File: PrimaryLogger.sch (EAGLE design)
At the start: 55 parts, among them J1 CONN_42.54_SCREW, J2 CONN_42.54_SCREW, J3 CONN_42.54_SCREW, J4 CONN_42.54_SCREW, J5 CONN_32.54_SCREW, Q1 DMG3404, Q2 DMG3404, U1 MIC2005, U2 MIC2091, U25 SN74AUP3G34DCU, U3 TPL5010DDC, U4 TXS0102DCU, U5 SN74LVC1G3157DRL, U6 TCS3400, U7 SHTC3DFN, U8 MCP23008QFN, U9 MCP7940SOIC

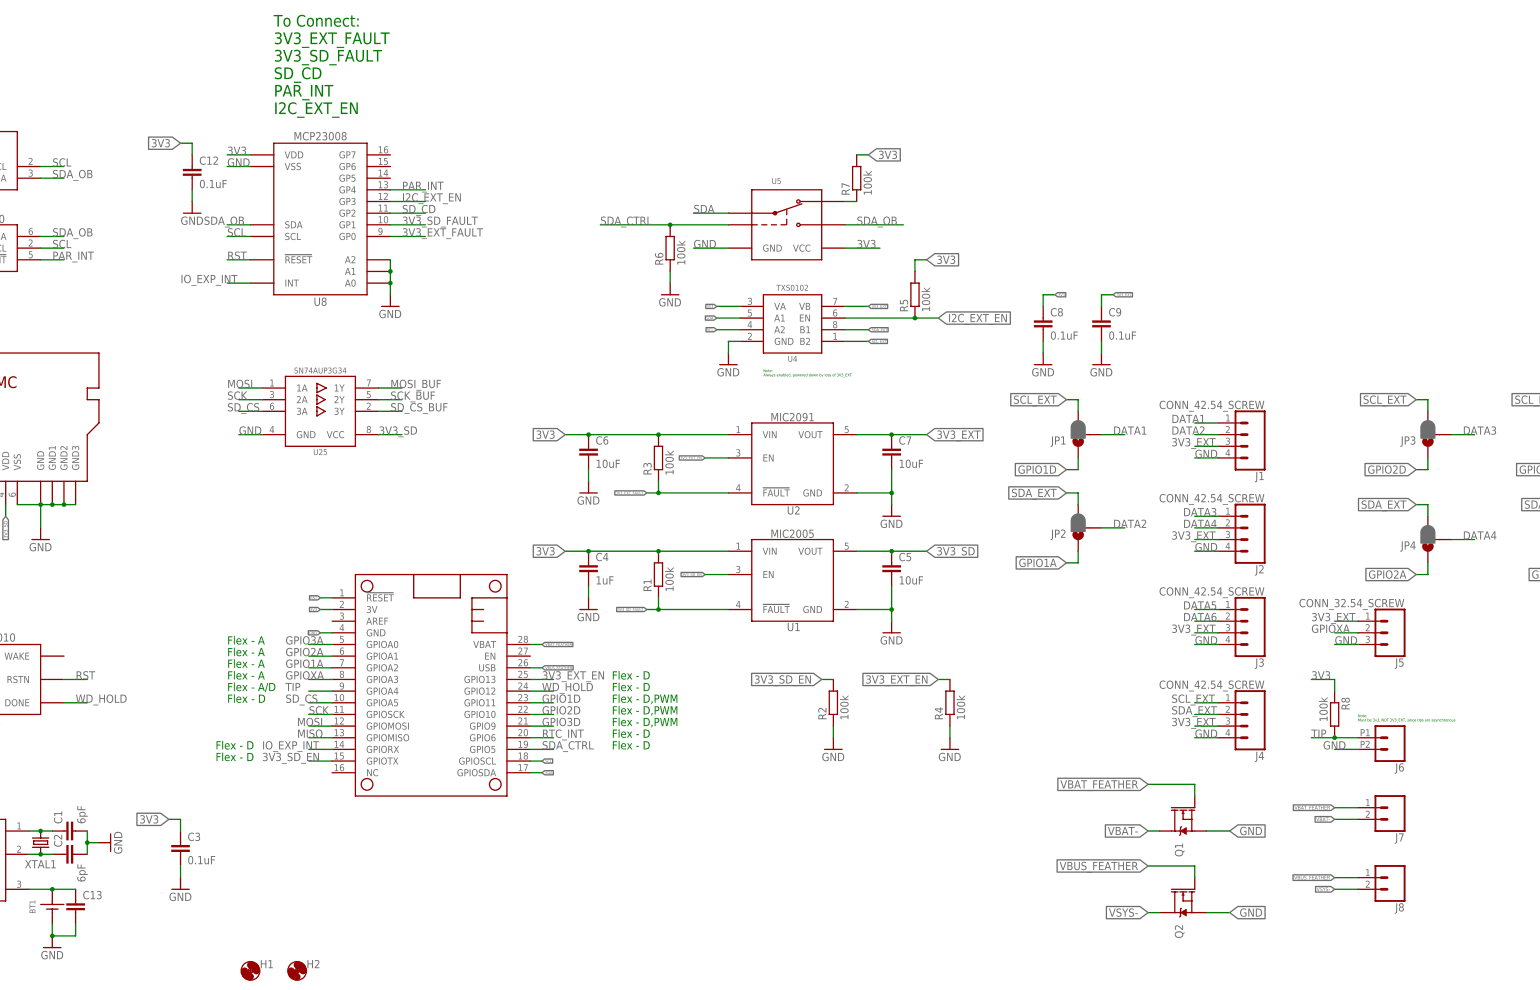
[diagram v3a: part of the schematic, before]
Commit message: Minor updates to layout
Added silk screen, added test points, other minor edits
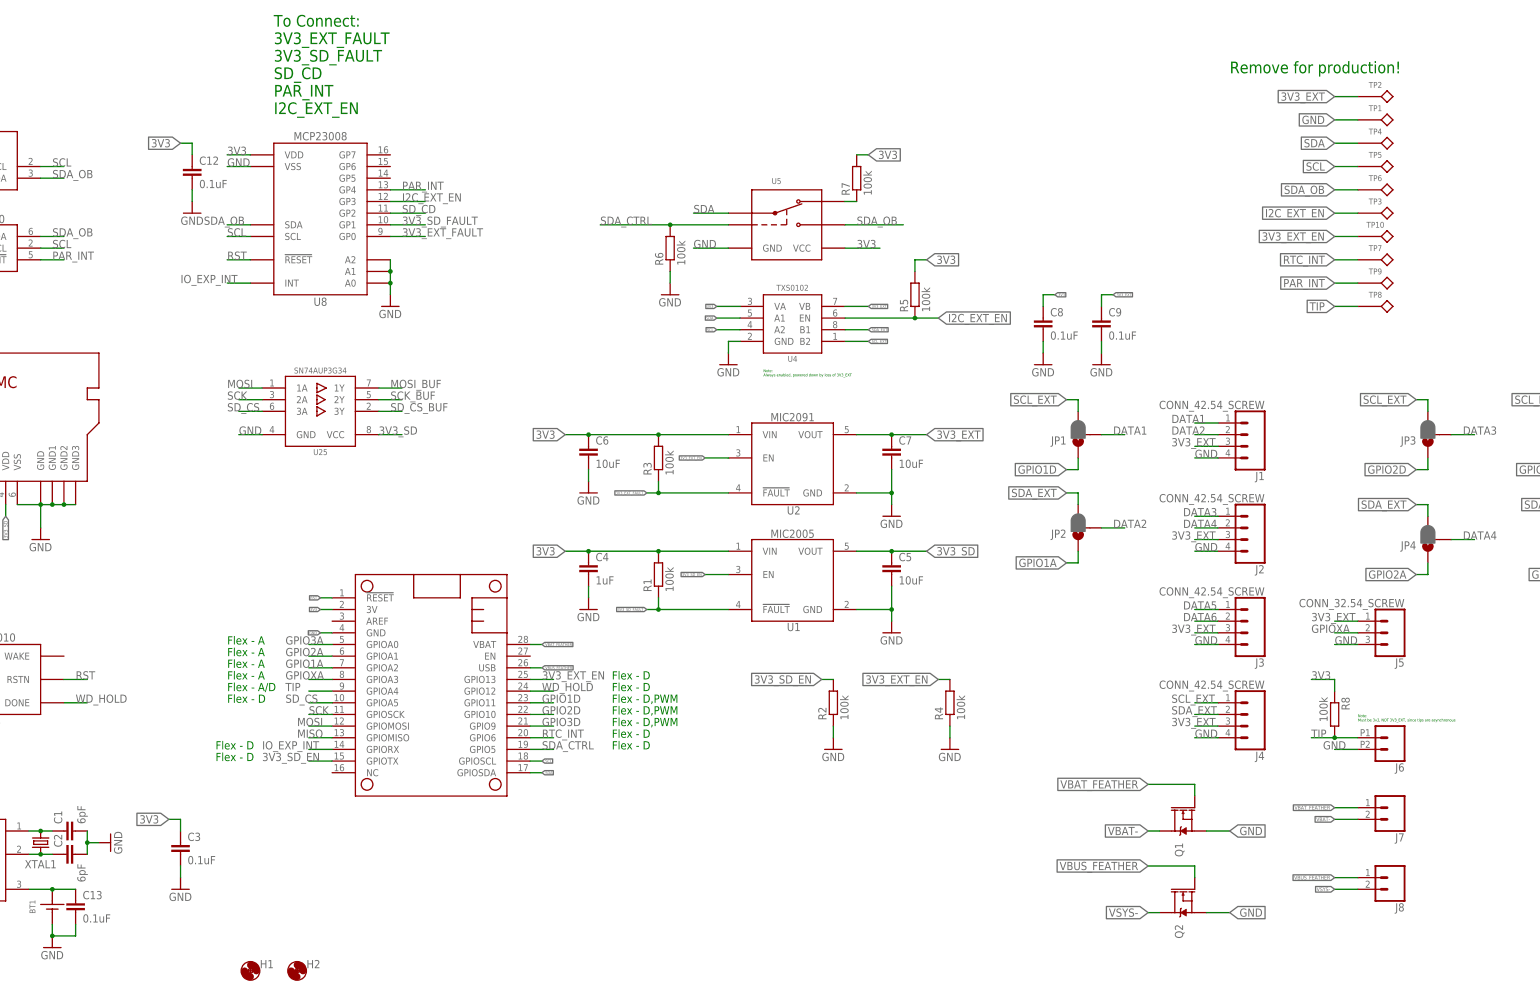
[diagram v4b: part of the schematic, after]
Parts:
- added TP1, TP10, TP2, TP3, TP4, TP5, TP6, TP7, TP8, TP9: TESTPOINTRCU, bschulz:TESTPOINTRCU
- C1, C2: device bschulz_passives:C-EUC0402 -> bschulz_passives:C-EU6PFC0402
- C13: value (none) -> 0.1uF
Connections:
- net 3V3_EXT: now also TP2.P$1
- net 3V3_EXT_EN: now also TP10.P$1
- net GND: now also TP1.P$1
- net I2C_EXT_EN: now also TP3.P$1
- net PAR_INT: now also TP9.P$1
- net RTC_INT: now also TP7.P$1
- net SCL: now also TP5.P$1
- net SDA: now also TP4.P$1
- net SDA_OB: now also TP6.P$1
- net TIP: now also TP8.P$1
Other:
- note added: "Remove for production!"
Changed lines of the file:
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@@
 <attribute name="MPN" value="Abracon"/>
 </part>
-<part name="C1" library="bschulz_passives" deviceset="C-EU" device="C0402" value="6pF"/>
-<part name="C2" library="bschulz_passives" deviceset="C-EU" device="C0402" value="6pF"/>
+<part name="C1" library="bschulz_passives" deviceset="C-EU" device="C0402" technology="6PF" value="6pF"/>
+<part name="C2" library="bschulz_passives" deviceset="C-EU" device="C0402" technology="6PF" value="6pF"/>
 <part name="GND1" library="supply1" library_urn="urn:adsk.eagle:library:371" deviceset="GND" device=""/>
 <part name="BT1" library="bschulz" deviceset="BATTERY_COIN" device="12MM"/>
@@
 <part name="Q1" library="bschulz" deviceset="MOSFET-NCH" device="-DMG3404L" value="DMG3404"/>
 <part name="Q2" library="bschulz" deviceset="MOSFET-NCH" device="-DMG3404L" value="DMG3404"/>
-<part name="C13" library="bschulz_passives" deviceset="C-EU" device="C0603" technology="0.1UF"/>
+<part name="C13" library="bschulz_passives" deviceset="C-EU" device="C0603" technology="0.1UF" value="0.1uF"/>
 <part name="H1" library="bschulz" deviceset="MOUNTING_HOLE" device="4_NP"/>
 <part name="H2" library="bschulz" deviceset="MOUNTING_HOLE" device="4_NP"/>
+<part name="TP2" library="bschulz" deviceset="TESTPOINT" device="RCU"/>
+<part name="TP1" library="bschulz" deviceset="TESTPOINT" device="RCU"/>
+<part name="TP4" library="bschulz" deviceset="TESTPOINT" device="RCU"/>
+<part name="TP5" library="bschulz" deviceset="TESTPOINT" device="RCU"/>
+<part name="TP6" library="bschulz" deviceset="TESTPOINT" device="RCU"/>
+<part name="TP3" library="bschulz" deviceset="TESTPOINT" device="RCU"/>
+<part name="TP10" library="bschulz" deviceset="TESTPOINT" device="RCU"/>
+<part name="TP7" library="bschulz" deviceset="TESTPOINT" device="RCU"/>
+<part name="TP9" library="bschulz" deviceset="TESTPOINT" device="RCU"/>
+<part name="TP8" library="bschulz" deviceset="TESTPOINT" device="RCU"/>
 </parts>
 <sheets>
@@
 <text x="172.72" y="71.12" size="1.778" layer="91">Flex - D,PWM</text>
 <text x="172.72" y="68.58" size="1.778" layer="91">Flex - D,PWM</text>
+<text x="307.34" y="210.82" size="2.54" layer="91">Remove for production!</text>
 </plain>
 <instances>
@@
 <attribute name="NAME" x="106.172" y="15.8242" size="1.778" layer="95"/>
 <attribute name="VALUE" x="106.172" y="12.7762" size="1.778" layer="96"/>
+</instance>
+<instance part="TP2" gate="G$1" x="335.28" y="205.74" smashed="yes" rot="R270">
+<attribute name="NAME" x="339.09" y="208.28" size="1.27" layer="95" align="center"/>
+</instance>
+<instance part="TP1" gate="G$1" x="335.28" y="200.66" smashed="yes" rot="R270">
+<attribute name="NAME" x="339.09" y="203.2" size="1.27" layer="95" align="center"/>
+</instance>
+<instance part="TP4" gate="G$1" x="335.28" y="195.58" smashed="yes" rot="R270">
+<attribute name="NAME" x="339.09" y="198.12" size="1.27" layer="95" align="center"/>
+</instance>
+<instance part="TP5" gate="G$1" x="335.28" y="190.5" smashed="yes" rot="R270">
+<attribute name="NAME" x="339.09" y="193.04" size="1.27" layer="95" align="center"/>
+</instance>
+<instance part="TP6" gate="G$1" x="335.28" y="185.42" smashed="yes" rot="R270">
+<attribute name="NAME" x="339.09" y="187.96" size="1.27" layer="95" align="center"/>
+</instance>
+<instance part="TP3" gate="G$1" x="335.28" y="180.34" smashed="yes" rot="R270">
+<attribute name="NAME" x="339.09" y="182.88" size="1.27" layer="95" align="center"/>
+</instance>
+<instance part="TP10" gate="G$1" x="335.28" y="175.26" smashed="yes" rot="R270">
+<attribute name="NAME" x="339.09" y="177.8" size="1.27" layer="95" align="center"/>
+</instance>
+<instance part="TP7" gate="G$1" x="335.28" y="170.18" smashed="yes" rot="R270">
+<attribute name="NAME" x="339.09" y="172.72" size="1.27" layer="95" align="center"/>
+</instance>
+<instance part="TP9" gate="G$1" x="335.28" y="165.1" smashed="yes" rot="R270">
+<attribute name="NAME" x="339.09" y="167.64" size="1.27" layer="95" align="center"/>
+</instance>
+<instance part="TP8" gate="G$1" x="335.28" y="160.02" smashed="yes" rot="R270">
+<attribute name="NAME" x="339.09" y="162.56" size="1.27" layer="95" align="center"/>
 </instance>
 </instances>
@@
 <label x="307.34" y="27.94" size="1.778" layer="95" xref="yes"/>
 </segment>
+<segment>
+<pinref part="TP1" gate="G$1" pin="P$1"/>
+<wire x1="335.28" y1="200.66" x2="330.2" y2="200.66" width="0.1524" layer="91"/>
+<label x="330.2" y="200.66" size="1.778" layer="95" rot="R180" xref="yes"/>
+</segment>
 </net>
 <net name="SDA" class="0">
@@
 <pinref part="U5" gate="G$1" pin="A"/>
 </segment>
+<segment>
+<pinref part="TP4" gate="G$1" pin="P$1"/>
+<wire x1="335.28" y1="195.58" x2="330.2" y2="195.58" width="0.1524" layer="91"/>
+<label x="330.2" y="195.58" size="1.778" layer="95" rot="R180" xref="yes"/>
+</segment>
 </net>
 <net name="SCL" class="0">
@@
 <label x="88.9" y="175.26" size="1.778" layer="95"/>
 </segment>
+<segment>
+<pinref part="TP5" gate="G$1" pin="P$1"/>
+<wire x1="335.28" y1="190.5" x2="330.2" y2="190.5" width="0.1524" layer="91"/>
+<label x="330.2" y="190.5" size="1.778" layer="95" rot="R180" xref="yes"/>
+</segment>
 </net>
 <net name="RTC_INT" class="0">
@@
 <wire x1="154.94" y1="66.04" x2="160.02" y2="66.04" width="0.1524" layer="91"/>
 <label x="157.48" y="66.04" size="1.778" layer="95"/>
+</segment>
+<segment>
+<pinref part="TP7" gate="G$1" pin="P$1"/>
+<wire x1="335.28" y1="170.18" x2="330.2" y2="170.18" width="0.1524" layer="91"/>
+<label x="330.2" y="170.18" size="1.778" layer="95" rot="R180" xref="yes"/>
 </segment>
 </net>
@@
 <label x="325.12" y="91.44" size="1.778" layer="95"/>
 </segment>
+<segment>
+<pinref part="TP2" gate="G$1" pin="P$1"/>
+<wire x1="335.28" y1="205.74" x2="330.2" y2="205.74" width="0.1524" layer="91"/>
+<label x="330.2" y="205.74" size="1.778" layer="95" rot="R180" xref="yes"/>
+</segment>
 </net>
 <net name="SDA_EXT" class="0">
@@
 <wire x1="154.94" y1="78.74" x2="160.02" y2="78.74" width="0.1524" layer="91"/>
 <label x="157.48" y="78.74" size="1.778" layer="95"/>
+</segment>
+<segment>
+<pinref part="TP10" gate="G$1" pin="P$1"/>
+<wire x1="335.28" y1="175.26" x2="330.2" y2="175.26" width="0.1524" layer="91"/>
+<label x="330.2" y="175.26" size="1.778" layer="95" rot="R180" xref="yes"/>
 </segment>
 </net>
@@
 <label x="83.82" y="177.8" size="1.778" layer="95"/>
 </segment>
+<segment>
+<pinref part="TP6" gate="G$1" pin="P$1"/>
+<wire x1="335.28" y1="185.42" x2="330.2" y2="185.42" width="0.1524" layer="91"/>
+<label x="330.2" y="185.42" size="1.778" layer="95" rot="R180" xref="yes"/>
+</segment>
 </net>
 <net name="SDA_CTRL" class="0">
@@
 <label x="127" y="185.42" size="1.778" layer="95"/>
 </segment>
+<segment>
+<pinref part="TP9" gate="G$1" pin="P$1"/>
+<wire x1="335.28" y1="165.1" x2="330.2" y2="165.1" width="0.1524" layer="91"/>
+<label x="330.2" y="165.1" size="1.778" layer="95" rot="R180" xref="yes"/>
+</segment>
 </net>
 <net name="TIP" class="0">
@@
 <label x="101.6" y="76.2" size="1.778" layer="95"/>
 </segment>
+<segment>
+<pinref part="TP8" gate="G$1" pin="P$1"/>
+<wire x1="335.28" y1="160.02" x2="330.2" y2="160.02" width="0.1524" layer="91"/>
+<label x="330.2" y="160.02" size="1.778" layer="95" rot="R180" xref="yes"/>
+</segment>
 </net>
 <net name="VSYS-" class="0">
@@
 <label x="127" y="182.88" size="1.778" layer="95"/>
 </segment>
-</net>
+<segment>
+<pinref part="TP3" gate="G$1" pin="P$1"/>
+<wire x1="335.28" y1="180.34" x2="330.2" y2="180.34" width="0.1524" layer="91"/>
+<label x="330.2" y="180.34" size="1.778" layer="95" rot="R180" xref="yes"/>
+</segment>
+</net>

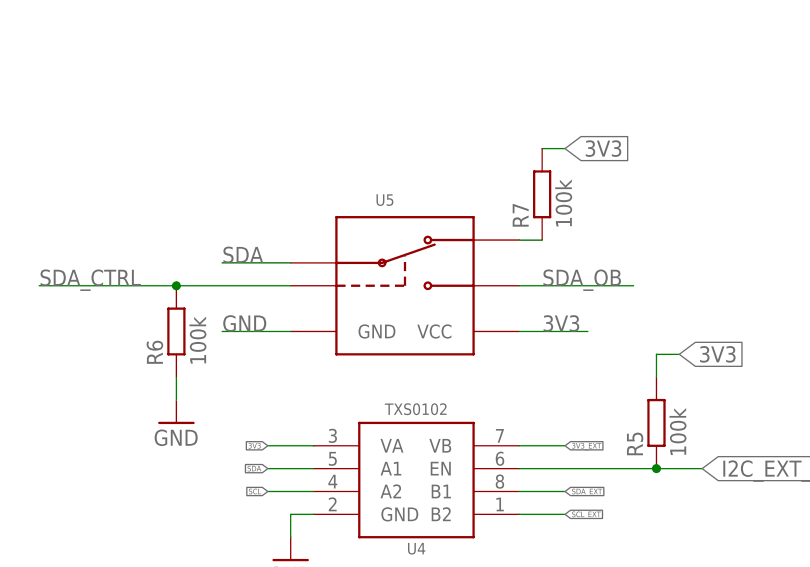
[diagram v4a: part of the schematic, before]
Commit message: Minor updates to make consistent with Soil Symbiont
Changed 10uF to 0805 and mux to SC-70 package
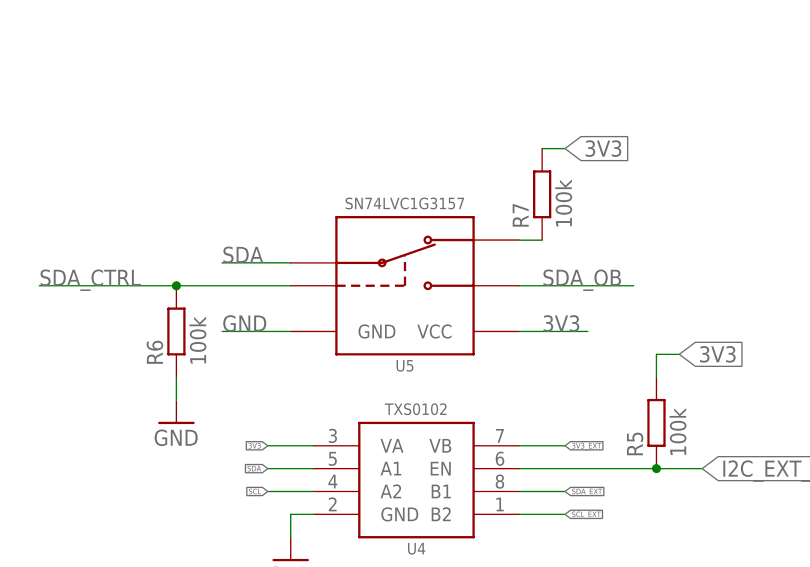
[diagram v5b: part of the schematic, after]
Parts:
- C5, C6, C7: device bschulz_passives:C-EU10UFC0603 -> bschulz_passives:C-EU10UFC0805
- U5: value SN74LVC1G3157DRL -> SN74LVC1G3157SC70; device bschulz:SN74LVC1G3157DRL -> bschulz:SN74LVC1G3157SC70
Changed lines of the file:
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@@
 <setting verticaltext="up"/>
 </settings>
-<grid distance="0.1" unitdist="inch" unit="mm" style="lines" multiple="1" display="no" altdistance="0.01" altunitdist="inch" altunit="inch"/>
+<grid distance="0.1" unitdist="inch" unit="inch" style="lines" multiple="1" display="no" altdistance="0.01" altunitdist="inch" altunit="inch"/>
 <layers>
 <layer number="1" name="Top" color="4" fill="1" visible="no" active="no"/>
@@
 <part name="U1" library="bschulz" deviceset="MIC2005" device=""/>
 <part name="C4" library="bschulz_passives" deviceset="C-EU" device="C0603" technology="1UF" value="1uF"/>
-<part name="C5" library="bschulz_passives" deviceset="C-EU" device="C0603" technology="10UF" value="10uF"/>
+<part name="C5" library="bschulz_passives" deviceset="C-EU" device="C0805" technology="10UF" value="10uF"/>
 <part name="GND5" library="supply1" library_urn="urn:adsk.eagle:library:371" deviceset="GND" device=""/>
 <part name="GND6" library="supply1" library_urn="urn:adsk.eagle:library:371" deviceset="GND" device=""/>
@@
 <part name="GND7" library="supply1" library_urn="urn:adsk.eagle:library:371" deviceset="GND" device=""/>
 <part name="U2" library="bschulz" deviceset="MIC209*" device="" technology="1" value="MIC2091"/>
-<part name="C6" library="bschulz_passives" deviceset="C-EU" device="C0603" technology="10UF" value="10uF"/>
-<part name="C7" library="bschulz_passives" deviceset="C-EU" device="C0603" technology="10UF" value="10uF"/>
+<part name="C6" library="bschulz_passives" deviceset="C-EU" device="C0805" technology="10UF" value="10uF"/>
+<part name="C7" library="bschulz_passives" deviceset="C-EU" device="C0805" technology="10UF" value="10uF"/>
 <part name="GND8" library="supply1" library_urn="urn:adsk.eagle:library:371" deviceset="GND" device=""/>
 <part name="GND9" library="supply1" library_urn="urn:adsk.eagle:library:371" deviceset="GND" device=""/>
@@
 <part name="JP5" library="SparkFun-Jumpers" library_urn="urn:adsk.eagle:library:528" deviceset="JUMPER-SMT_3_1-NC_PASTE" device="_SILK" package3d_urn="urn:adsk.eagle:package:39293/1"/>
 <part name="JP6" library="SparkFun-Jumpers" library_urn="urn:adsk.eagle:library:528" deviceset="JUMPER-SMT_3_1-NC_PASTE" device="_SILK" package3d_urn="urn:adsk.eagle:package:39293/1"/>
-<part name="U5" library="bschulz" deviceset="SN74LVC1G3157" device="DRL"/>
+<part name="U5" library="bschulz" deviceset="SN74LVC1G3157" device="SC70" value="SN74LVC1G3157SC70"/>
 <part name="R6" library="bschulz_passives" deviceset="R-EU_" device="R0603" technology="100K" value="100k"/>
 <part name="GND17" library="supply1" library_urn="urn:adsk.eagle:library:371" deviceset="GND" device=""/>
@@
 </instance>
 <instance part="U5" gate="G$1" x="210.82" y="180.34" smashed="yes">
-<attribute name="NAME" x="207.518" y="186.69" size="1.27" layer="96"/>
+<attribute name="NAME" x="210.82" y="168.91" size="1.27" layer="96" align="center"/>
+<attribute name="DISP" x="210.82" y="186.944" size="1.27" layer="95" ratio="15" align="center"/>
 </instance>
 <instance part="R6" gate="G$1" x="185.42" y="172.72" smashed="yes" rot="R90">

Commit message: Minor part value and silkscreen updates, gerbers generated
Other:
- note added: "Connectors/Mounting"
- note added: "Digital Core"
- note added: "Interface"
- note added: "Power"
- note added: "Sensors"
- note removed: "To Connect: 3V3_EXT_FAULT 3V3_SD_FAULT SD_CD PAR_INT I2C_EXT_EN"
